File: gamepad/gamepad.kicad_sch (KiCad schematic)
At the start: 6 parts, among them U1 NE555P

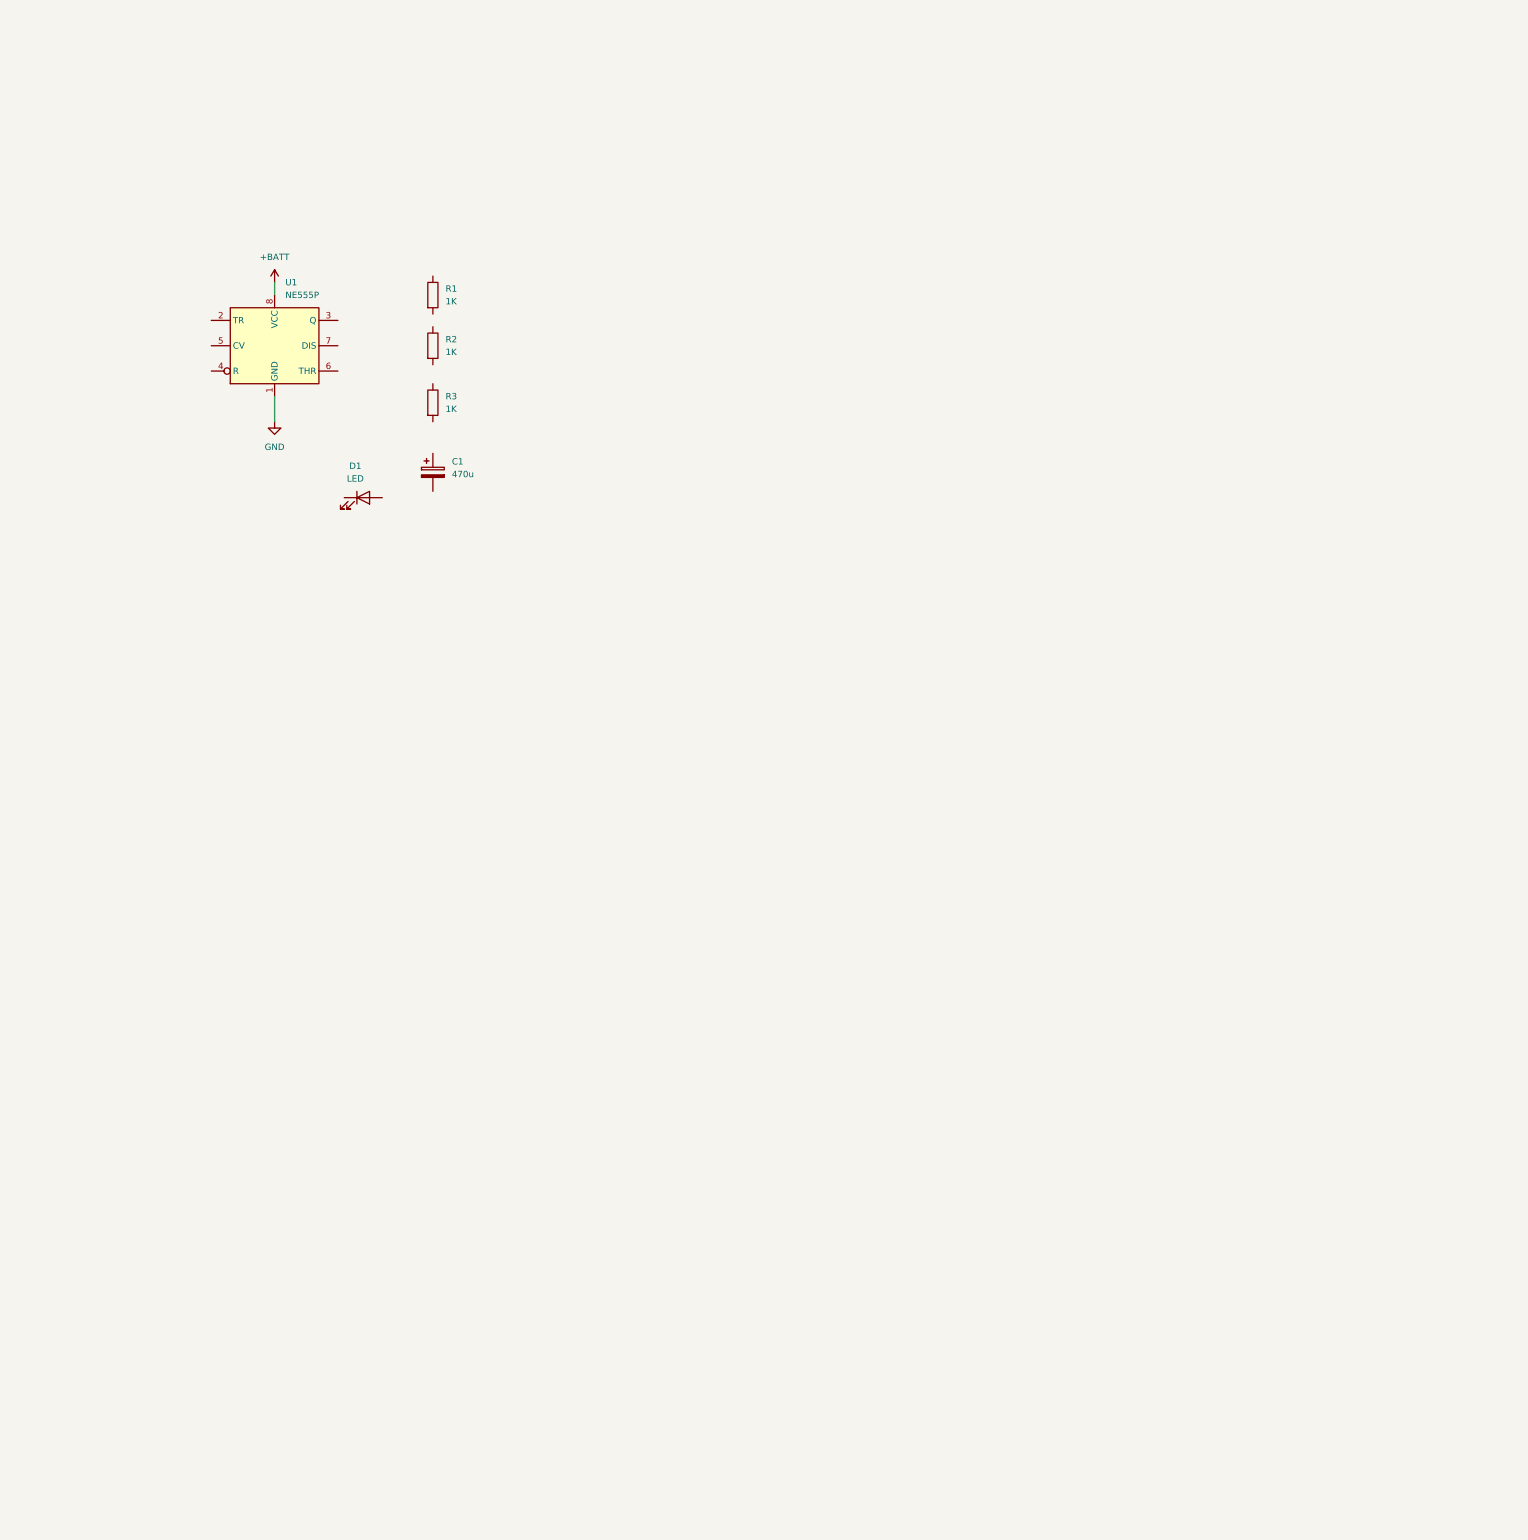
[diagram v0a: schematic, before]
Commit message: buttons have been placed
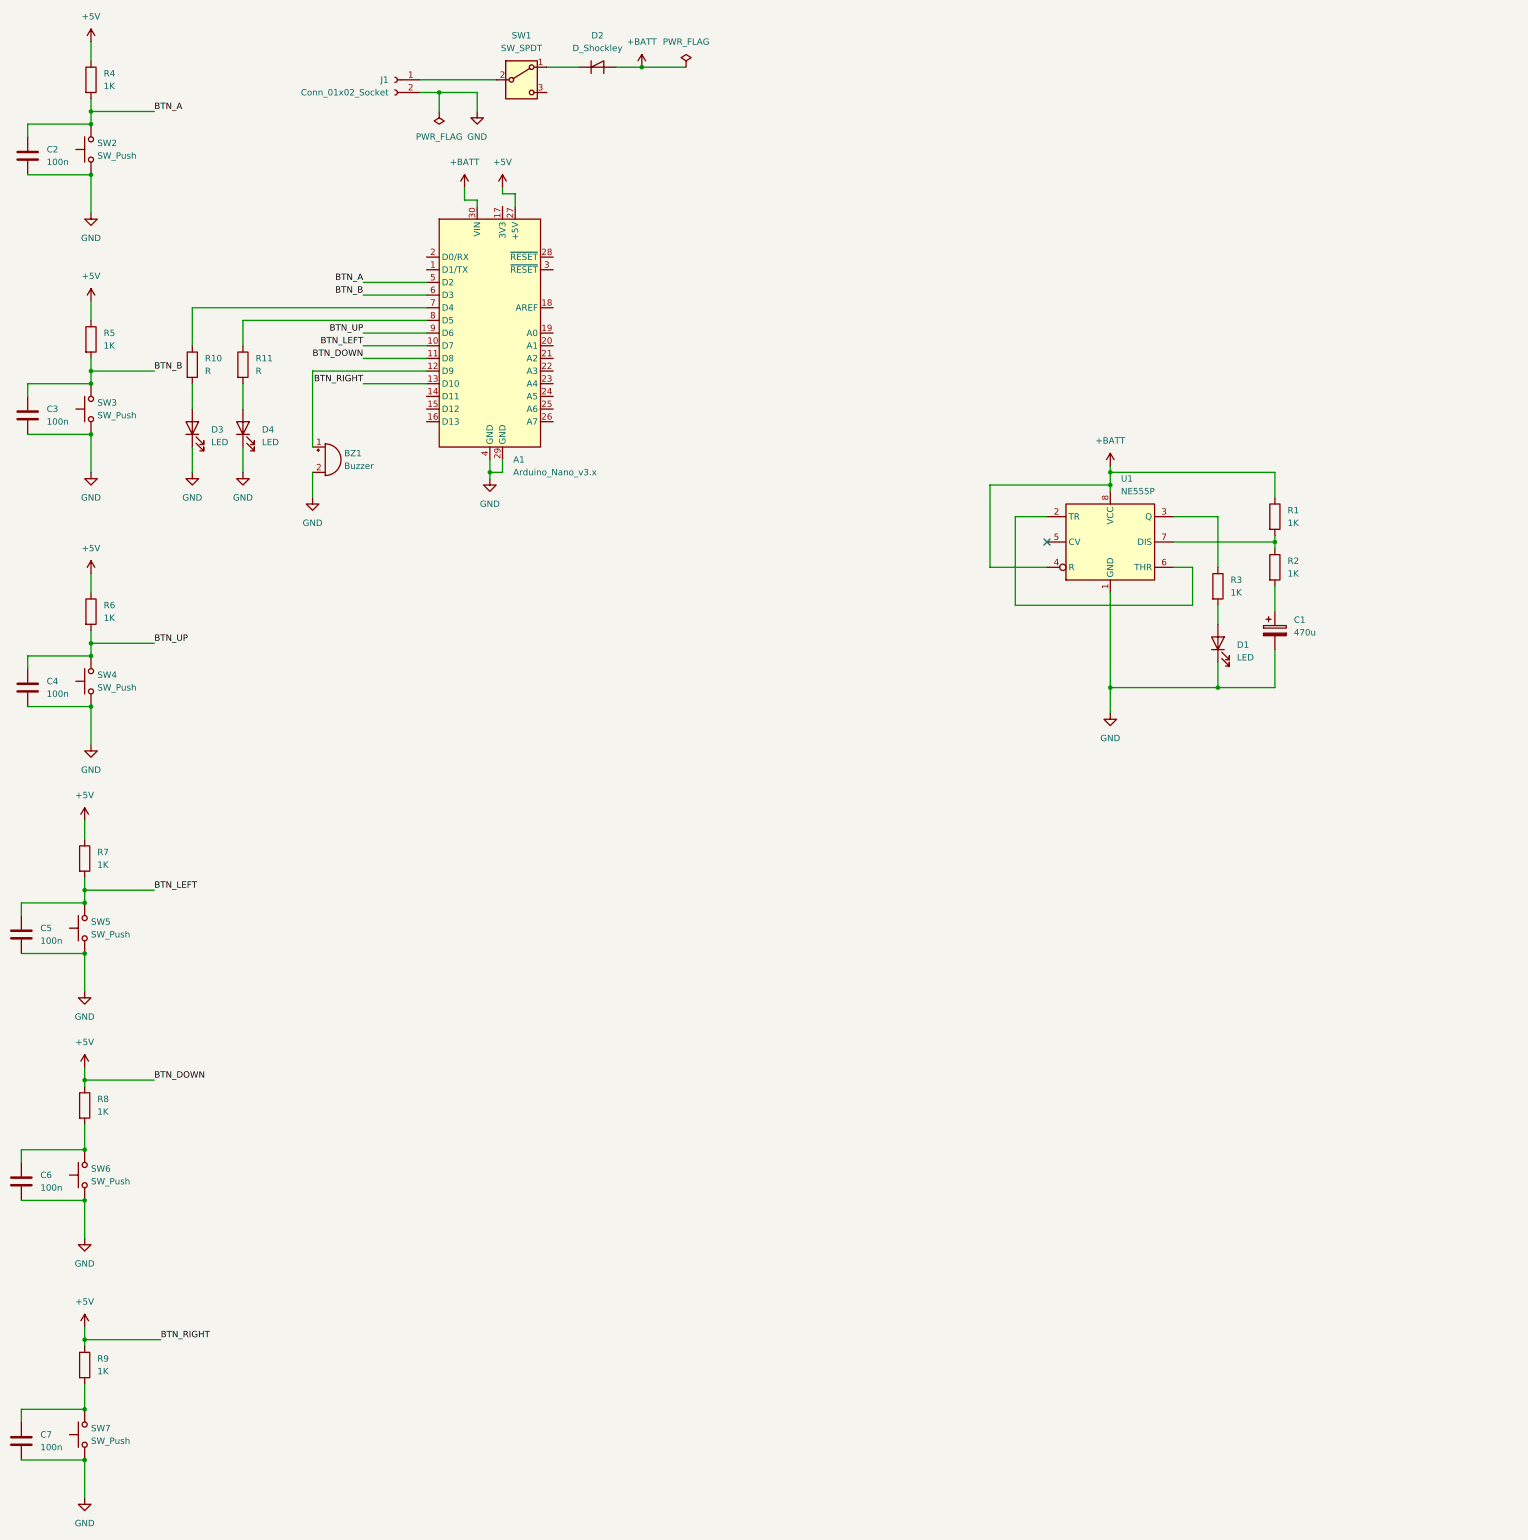
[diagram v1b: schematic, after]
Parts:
- added A1: Arduino_Nano_v3.x, Module:Arduino_Nano, symbol MCU_Module:Arduino_Nano_v3.x
- added BZ1: Buzzer, symbol Device:Buzzer
- added C2, C3, C4, C5, C6, C7: 100n, symbol Device:C
- added D2: D_Shockley, symbol Device:D_Shockley
- added D3, D4: LED, symbol Device:LED
- added J1: Conn_01x02_Socket, symbol Connector:Conn_01x02_Socket
- added R10, R11: R, symbol Device:R
- added R4, R5, R6, R7, R8, R9: 1K, symbol Device:R
- added SW1: SW_SPDT, symbol Switch:SW_SPDT
- added SW2, SW3, SW4, SW5, SW6, SW7: SW_Push, symbol Switch:SW_Push
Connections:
- net +BATT: now also R1.1, U1.4 (R), A1.30 (VIN), D2.2 (A)
- net GND: now also C1.2, D1.1 (K), A1.29 (GND), A1.4 (GND), BZ1.2 (-), C2.2, C3.2, C4.2, C5.2, C6.2, C7.2, D3.1 (K), D4.1 (K), J1.2 (Pin_2), SW2.1, SW3.1, SW4.1, SW5.1, SW6.1, SW7.1
- net at R3.1: now also U1.3 (Q)
- net at R3.2: now also D1.2 (A)
- net at R2.1: now also R1.2, U1.7 (DIS)
- net at R2.2: now also C1.1
- net at U1.2 (TR): now also U1.6 (THR)
- new net: J1.1 (Pin_1), SW1.2 (B)
- new net: D2.1 (K), SW1.1 (A)
- new net: D3.2 (A), R10.2
- new net: C6.1, R8.2, SW6.2
- new net: A1.7 (D4), R10.1
- new net: A1.12 (D9), BZ1.1 (+)
- new net: C7.1, R9.2, SW7.2
- new net: A1.8 (D5), R11.1
- new net: D4.2 (A), R11.2
- new net +5V: A1.11 (D8), A1.13 (D10), A1.27 (+5V), R4.1, R5.1, R6.1, R7.1, R8.1, R9.1
- new net BTN_A: A1.5 (D2), C2.1, R4.2, SW2.2
- new net BTN_B: A1.6 (D3), C3.1, R5.2, SW3.2
- new net BTN_LEFT: A1.10 (D7), C5.1, R7.2, SW5.2
- new net BTN_UP: A1.9 (D6), C4.1, R6.2, SW4.2
- no-connect marks 0 -> 1
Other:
- moved on the sheet: C1, D1, R1, R2, R3, U1

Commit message: schematic is done
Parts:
- removed D2: D_Shockley, symbol Device:D_Shockley
- added D2: BAT42, Diode_THT:D_DO-35_SOD27_P7.62mm_Horizontal, symbol Diode:BAT42
- added U2: I2C_OLED_MODULE, symbol oled_module:i2c_oled_module
- BZ1: footprint (none) -> Buzzer_Beeper:Buzzer_12x9.5RM7.6
- C2, C3, C4, C5, C6, C7: footprint (none) -> Capacitor_THT:C_Disc_D4.7mm_W2.5mm_P5.00mm
- D1, D3, D4: footprint (none) -> LED_THT:LED_D5.0mm
- J1: footprint (none) -> Connector_Molex:Molex_Micro-Latch_53254-0270_1x02_P2.00mm_Horizontal
- R1, R2, R3, R4, R5, R6, R7, R8, R9: footprint (none) -> Resistor_THT:R_Axial_DIN0207_L6.3mm_D2.5mm_P7.62mm_Horizontal
- R10, R11: value R -> 1K; footprint (none) -> Resistor_THT:R_Axial_DIN0207_L6.3mm_D2.5mm_P7.62mm_Horizontal
- SW2, SW3, SW4, SW5, SW6, SW7: footprint (none) -> Button_Switch_THT:SW_PUSH_6mm
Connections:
- net +5V: now also U2.2 (VCC)
- net +BATT: now also D2.1 (K)
- net GND: now also U2.1 (GND)
- net at C1.1, R2.2: now also U1.2 (TR), U1.6 (THR)
- net at SW1.1 (A): now also D2.2 (A)
- net at A1.23 (A4): now also U2.4 (SDA)
- net at A1.24 (A5): now also U2.3 (SCL)
- no-connect marks 1 -> 17
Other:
- moved on the sheet: A1, BZ1, C1, C5, C6, C7, D1, D3, D4, J1, R1, R10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

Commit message: footprints assigned
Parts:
- C1: footprint (none) -> Capacitor_THT:CP_Radial_D6.3mm_P2.50mm
- SW1: footprint (none) -> spdt_slide_switch:spdt_slide_switch
- U2: footprint (none) -> oled_module:i2c_oled_module

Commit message: components placed on PCB
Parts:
- added H1, H2, H3, H4: MountingHole, MountingHole:MountingHole_2.5mm, symbol Mechanical:MountingHole
